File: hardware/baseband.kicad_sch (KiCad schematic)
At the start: 36 parts, among them U501 MCP4551-103, U502 MCP455x, U6 MCP6002, U7 MCP6002

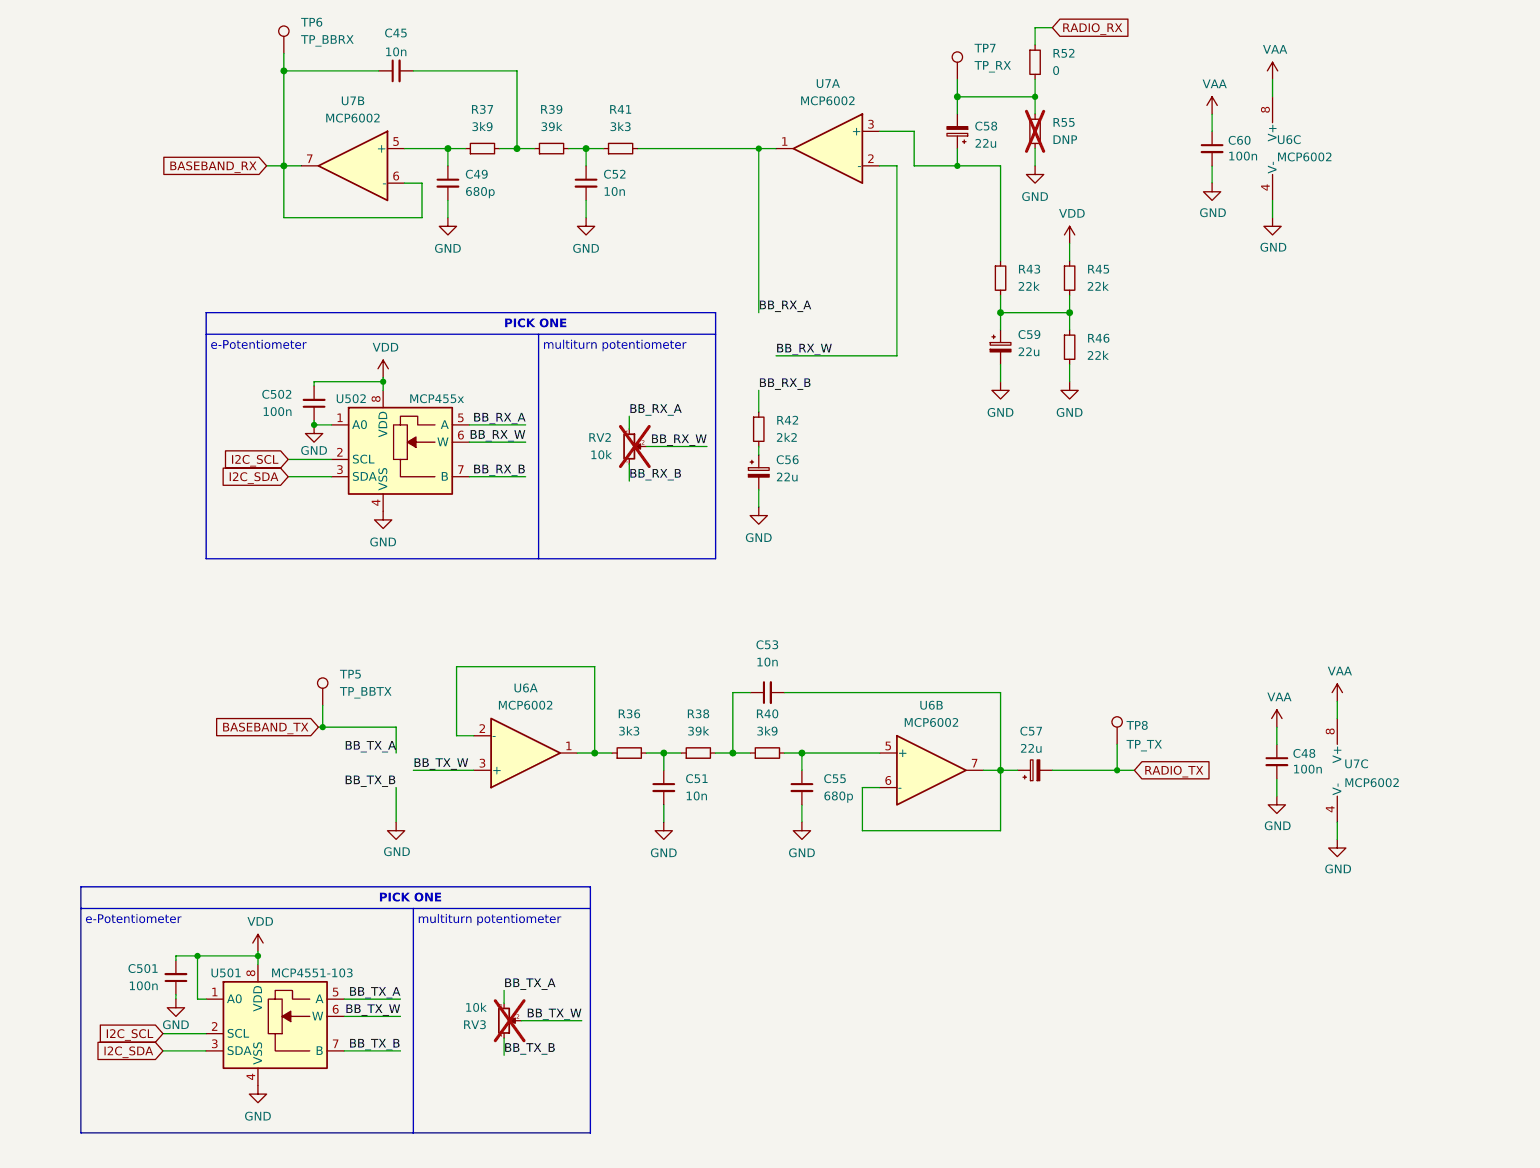
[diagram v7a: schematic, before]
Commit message: Replaced pkl symbols with kicad library symbols
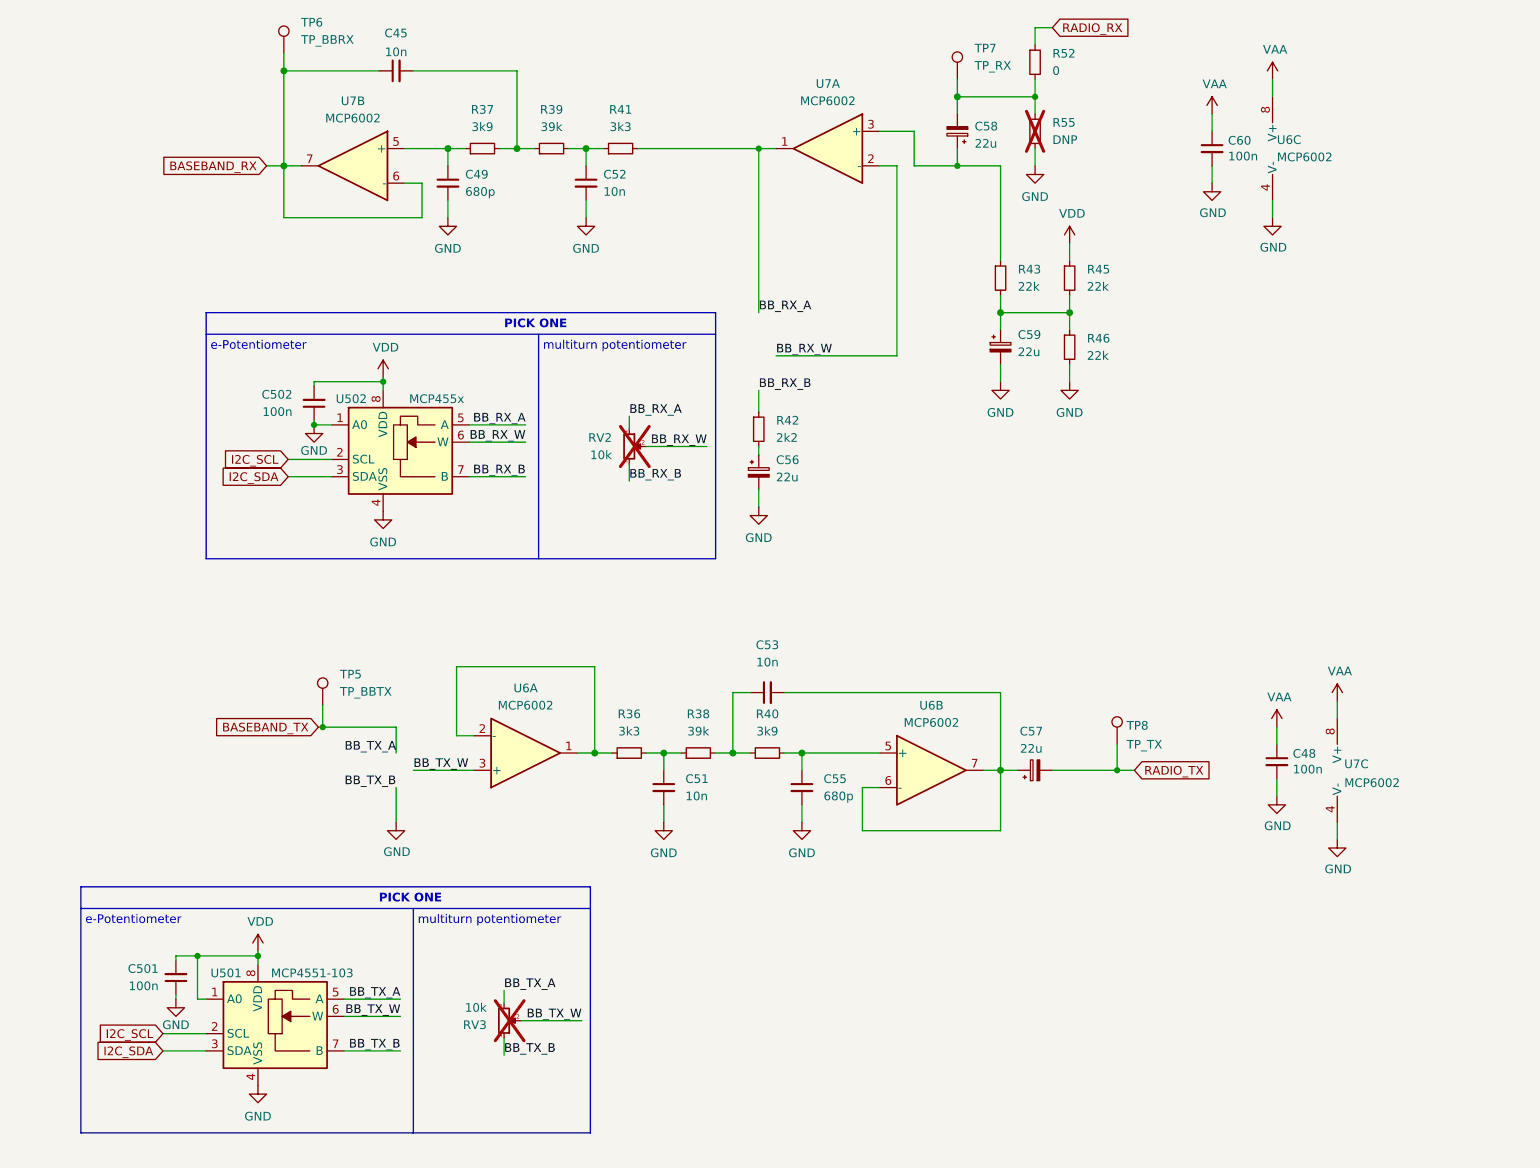
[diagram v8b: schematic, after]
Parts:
- C45, C48, C49, C51, C52, C53, C55, C60: symbol pkl_device:pkl_C_Small -> Device:C_Small
- C56, C57, C58, C59: symbol pkl_device:pkl_CP_Small -> Device:C_Polarized_Small
- R36, R37, R38, R39, R40, R41, R42, R43, R45, R46, R52, R55: symbol pkl_device:pkl_R_Small -> Device:R_Small
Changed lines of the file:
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@@
     )
   )
-  (symbol (lib_id "pkl_device:pkl_R_Small") (at 180.34 36.83 0) (unit 1)
+  (symbol (lib_id "Device:R_Small") (at 180.34 36.83 0) (unit 1)
     (in_bom no) (on_board yes) (dnp yes) (fields_autoplaced)
     (property "Reference" "R55" (at 182.88 35.56 0)
@@
     )
   )
-  (symbol (lib_id "pkl_device:pkl_CP_Small") (at 139.7 86.995 0) (unit 1)
+  (symbol (lib_id "Device:C_Polarized_Small") (at 139.7 86.995 0) (unit 1)
     (in_bom yes) (on_board yes) (dnp no) (fields_autoplaced)
     (property "Reference" "C56" (at 142.24 85.1789 0)
@@
     )
   )
-  (symbol (lib_id "pkl_device:pkl_R_Small") (at 185.42 68.58 0) (unit 1)
+  (symbol (lib_id "Device:R_Small") (at 185.42 68.58 0) (unit 1)
     (in_bom yes) (on_board yes) (dnp no) (fields_autoplaced)
     (property "Reference" "R46" (at 187.96 67.31 0)
@@
     )
   )
-  (symbol (lib_id "pkl_device:pkl_C_Small") (at 206.375 39.37 0) (unit 1)
+  (symbol (lib_id "Device:C_Small") (at 206.375 39.37 0) (unit 1)
     (in_bom yes) (on_board yes) (dnp no)
     (property "Reference" "C60" (at 208.7118 38.2016 0)
@@
     )
   )
-  (symbol (lib_id "pkl_device:pkl_C_Small") (at 146.05 133.35 0) (unit 1)
+  (symbol (lib_id "Device:C_Small") (at 146.05 133.35 0) (unit 1)
     (in_bom yes) (on_board yes) (dnp no) (fields_autoplaced)
     (property "Reference" "C55" (at 149.225 132.0863 0)
@@
     )
   )
-  (symbol (lib_id "pkl_device:pkl_CP_Small") (at 180.34 130.81 90) (unit 1)
+  (symbol (lib_id "Device:C_Polarized_Small") (at 180.34 130.81 90) (unit 1)
     (in_bom yes) (on_board yes) (dnp no) (fields_autoplaced)
     (property "Reference" "C57" (at 179.7939 125.095 90)
@@
     )
   )
-  (symbol (lib_id "pkl_device:pkl_C_Small") (at 93.98 44.45 0) (unit 1)
+  (symbol (lib_id "Device:C_Small") (at 93.98 44.45 0) (unit 1)
     (in_bom yes) (on_board yes) (dnp no) (fields_autoplaced)
     (property "Reference" "C49" (at 96.52 43.1863 0)
@@
     )
   )
-  (symbol (lib_id "pkl_device:pkl_R_Small") (at 175.26 58.42 0) (unit 1)
+  (symbol (lib_id "Device:R_Small") (at 175.26 58.42 0) (unit 1)
     (in_bom yes) (on_board yes) (dnp no) (fields_autoplaced)
     (property "Reference" "R43" (at 177.8 57.15 0)
@@
     )
   )
-  (symbol (lib_id "pkl_device:pkl_R_Small") (at 99.06 39.37 90) (unit 1)
+  (symbol (lib_id "Device:R_Small") (at 99.06 39.37 90) (unit 1)
     (in_bom yes) (on_board yes) (dnp no) (fields_autoplaced)
     (property "Reference" "R37" (at 99.06 33.655 90)
@@
     )
   )
-  (symbol (lib_id "pkl_device:pkl_R_Small") (at 185.42 58.42 0) (unit 1)
+  (symbol (lib_id "Device:R_Small") (at 185.42 58.42 0) (unit 1)
     (in_bom yes) (on_board yes) (dnp no) (fields_autoplaced)
     (property "Reference" "R45" (at 187.96 57.15 0)
@@
     )
   )
-  (symbol (lib_id "pkl_device:pkl_R_Small") (at 119.38 39.37 90) (unit 1)
+  (symbol (lib_id "Device:R_Small") (at 119.38 39.37 90) (unit 1)
     (in_bom yes) (on_board yes) (dnp no) (fields_autoplaced)
     (property "Reference" "R41" (at 119.38 33.655 90)
@@
     )
   )
-  (symbol (lib_id "pkl_device:pkl_CP_Small") (at 175.26 68.58 0) (unit 1)
+  (symbol (lib_id "Device:C_Polarized_Small") (at 175.26 68.58 0) (unit 1)
     (in_bom yes) (on_board yes) (dnp no) (fields_autoplaced)
     (property "Reference" "C59" (at 177.8 66.7639 0)
@@
     )
   )
-  (symbol (lib_id "pkl_device:pkl_R_Small") (at 139.7 80.645 0) (unit 1)
+  (symbol (lib_id "Device:R_Small") (at 139.7 80.645 0) (unit 1)
     (in_bom yes) (on_board yes) (dnp no)
     (property "Reference" "R42" (at 142.24 79.375 0)
@@
     )
   )
-  (symbol (lib_id "pkl_device:pkl_R_Small") (at 180.34 26.67 0) (unit 1)
+  (symbol (lib_id "Device:R_Small") (at 180.34 26.67 0) (unit 1)
     (in_bom yes) (on_board yes) (dnp no) (fields_autoplaced)
     (property "Reference" "R52" (at 182.88 25.4 0)
@@
     )
   )
-  (symbol (lib_id "pkl_device:pkl_C_Small") (at 114.3 44.45 0) (unit 1)
+  (symbol (lib_id "Device:C_Small") (at 114.3 44.45 0) (unit 1)
     (in_bom yes) (on_board yes) (dnp no) (fields_autoplaced)
     (property "Reference" "C52" (at 116.84 43.1863 0)
@@
     )
   )
-  (symbol (lib_id "pkl_device:pkl_C_Small") (at 140.97 119.38 90) (unit 1)
+  (symbol (lib_id "Device:C_Small") (at 140.97 119.38 90) (unit 1)
     (in_bom yes) (on_board yes) (dnp no) (fields_autoplaced)
     (property "Reference" "C53" (at 140.9763 112.395 90)
@@
     )
   )
-  (symbol (lib_id "pkl_device:pkl_R_Small") (at 120.65 128.27 90) (unit 1)
+  (symbol (lib_id "Device:R_Small") (at 120.65 128.27 90) (unit 1)
     (in_bom yes) (on_board yes) (dnp no) (fields_autoplaced)
     (property "Reference" "R36" (at 120.65 122.555 90)
@@
     )
   )
-  (symbol (lib_id "pkl_device:pkl_C_Small") (at 86.36 27.94 90) (unit 1)
+  (symbol (lib_id "Device:C_Small") (at 86.36 27.94 90) (unit 1)
     (in_bom yes) (on_board yes) (dnp no)
     (property "Reference" "C45" (at 86.36 22.4113 90)
@@
     )
   )
-  (symbol (lib_id "pkl_device:pkl_R_Small") (at 109.22 39.37 90) (unit 1)
+  (symbol (lib_id "Device:R_Small") (at 109.22 39.37 90) (unit 1)
     (in_bom yes) (on_board yes) (dnp no) (fields_autoplaced)
     (property "Reference" "R39" (at 109.22 33.655 90)
@@
     )
   )
-  (symbol (lib_id "pkl_device:pkl_C_Small") (at 215.9 129.54 0) (unit 1)
+  (symbol (lib_id "Device:C_Small") (at 215.9 129.54 0) (unit 1)
     (in_bom yes) (on_board yes) (dnp no)
     (property "Reference" "C48" (at 218.2368 128.3716 0)
@@
     )
   )
-  (symbol (lib_id "pkl_device:pkl_R_Small") (at 140.97 128.27 90) (unit 1)
+  (symbol (lib_id "Device:R_Small") (at 140.97 128.27 90) (unit 1)
     (in_bom yes) (on_board yes) (dnp no) (fields_autoplaced)
     (property "Reference" "R40" (at 140.97 122.555 90)
@@
     )
   )
-  (symbol (lib_id "pkl_device:pkl_C_Small") (at 125.73 133.35 0) (unit 1)
+  (symbol (lib_id "Device:C_Small") (at 125.73 133.35 0) (unit 1)
     (in_bom yes) (on_board yes) (dnp no) (fields_autoplaced)
     (property "Reference" "C51" (at 128.905 132.0863 0)
@@
     )
   )
-  (symbol (lib_id "pkl_device:pkl_CP_Small") (at 168.91 36.83 180) (unit 1)
+  (symbol (lib_id "Device:C_Polarized_Small") (at 168.91 36.83 180) (unit 1)
     (in_bom yes) (on_board yes) (dnp no) (fields_autoplaced)
     (property "Reference" "C58" (at 171.45 36.1061 0)
@@
     )
   )
-  (symbol (lib_id "pkl_device:pkl_R_Small") (at 130.81 128.27 90) (unit 1)
+  (symbol (lib_id "Device:R_Small") (at 130.81 128.27 90) (unit 1)
     (in_bom yes) (on_board yes) (dnp no) (fields_autoplaced)
     (property "Reference" "R38" (at 130.81 122.555 90)
